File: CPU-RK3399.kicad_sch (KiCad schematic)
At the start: 0 parts

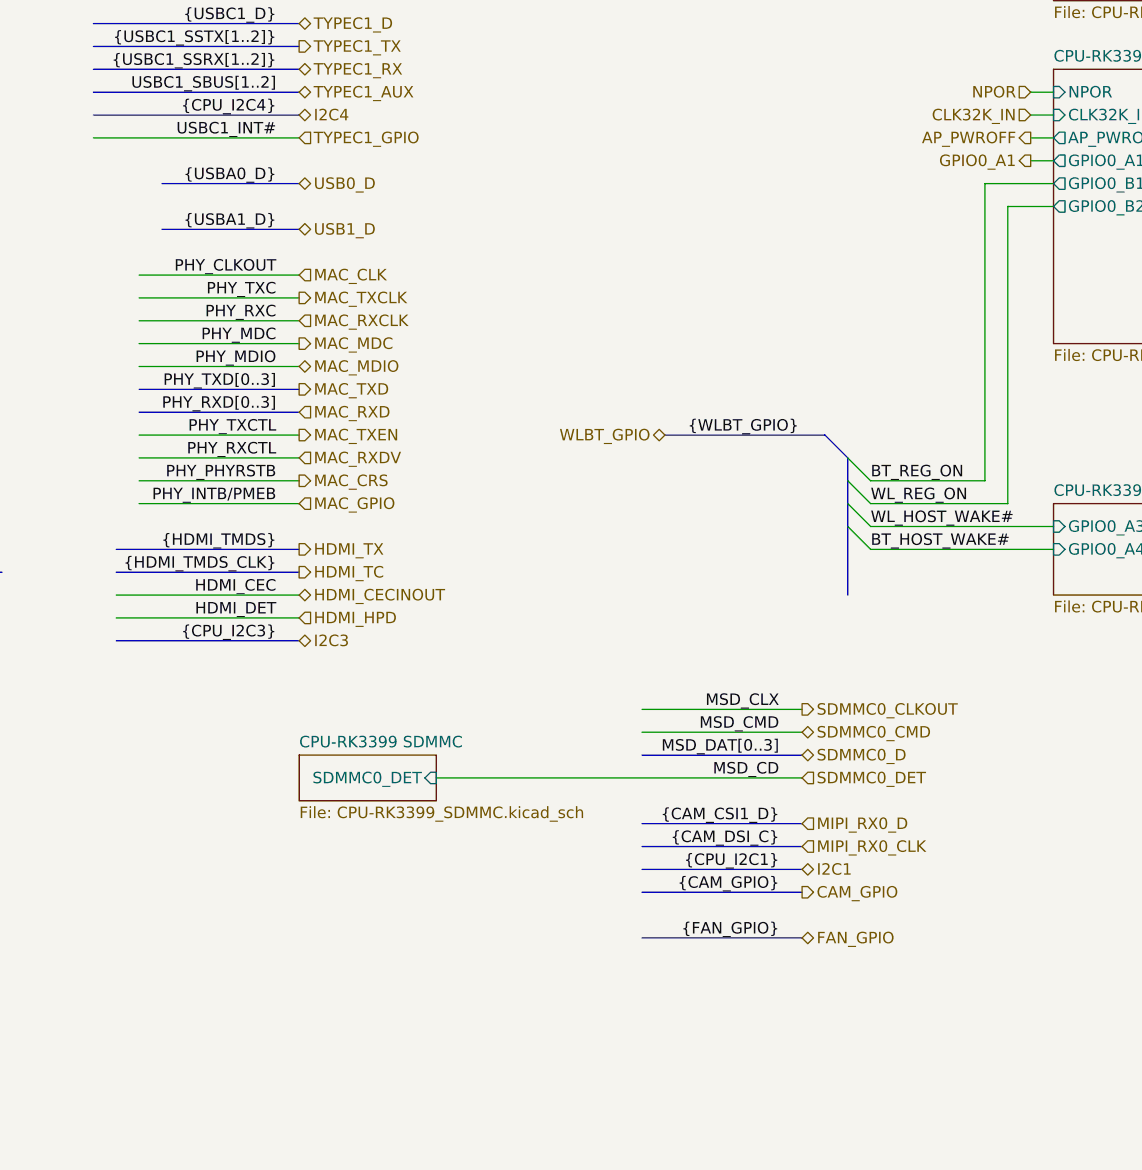
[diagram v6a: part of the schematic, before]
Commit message: design USB
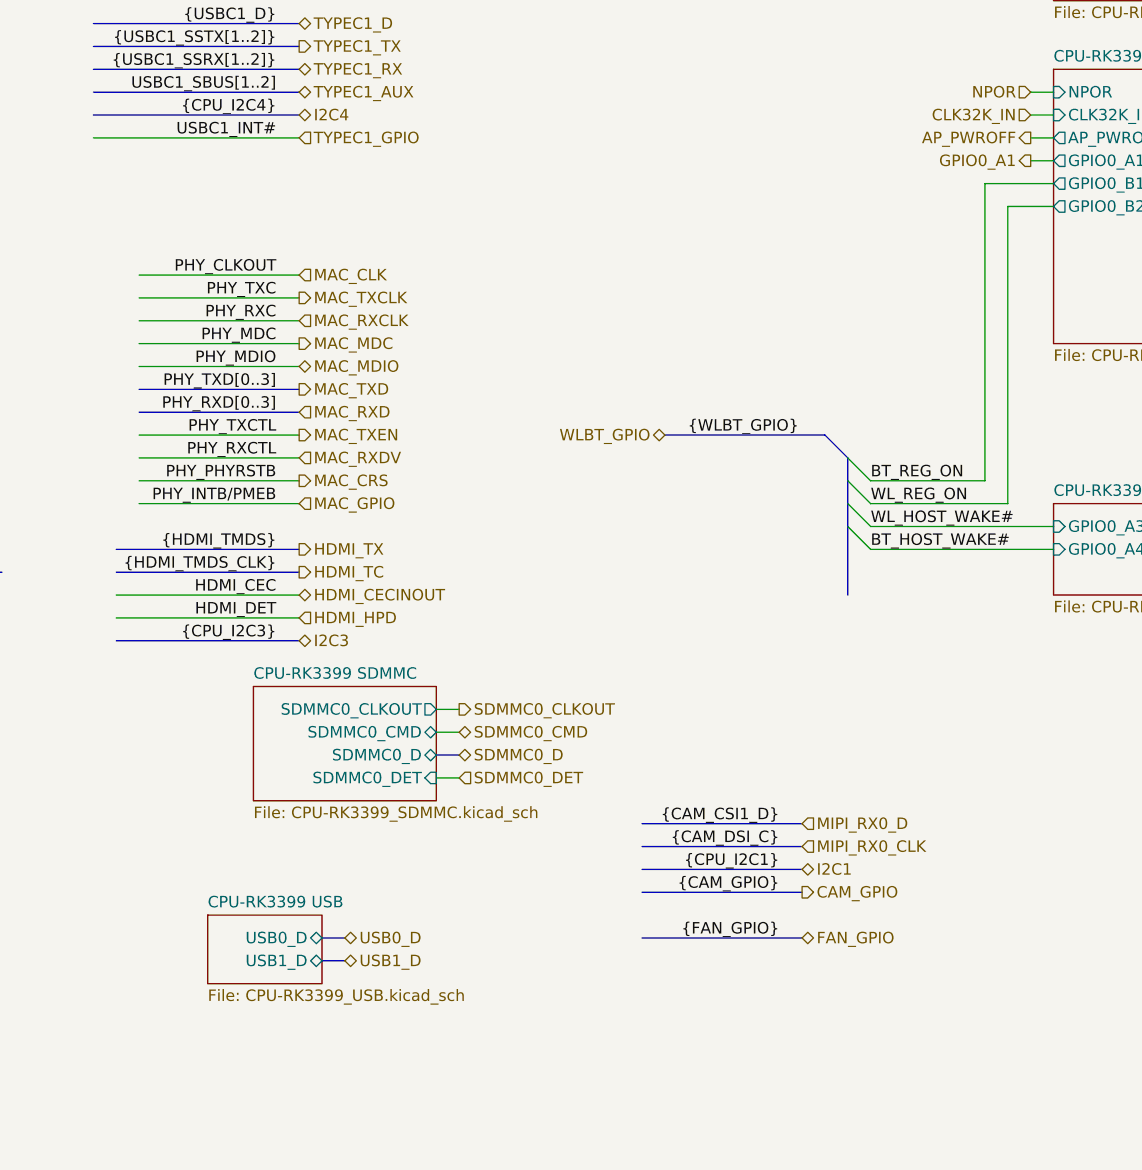
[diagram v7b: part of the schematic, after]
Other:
- added sheet CPU-RK3399 USB (CPU-RK3399_USB.kicad_sch)
- sheet CPU-RK3399 SDMMC ports: added SDMMC0_CLKOUT, SDMMC0_CMD, SDMMC0_D; removed none
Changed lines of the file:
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@@
 		)
 	)
-	(wire
-		(pts
-			(xy 208.28 134.62) (xy 190.5 134.62)
-		)
-		(stroke
-			(width 0)
-			(type default)
-		)
-	)
 	(bus
 		(pts
@@
 		)
 	)
-	(bus
-		(pts
-			(xy 137.16 73.66) (xy 152.4 73.66)
-		)
-		(stroke
-			(width 0)
-			(type default)
-		)
-	)
 	(wire
 		(pts
@@
 	(bus
 		(pts
+			(xy 154.94 160.02) (xy 157.48 160.02)
+		)
+		(stroke
+			(width 0)
+			(type default)
+		)
+	)
+	(bus
+		(pts
 			(xy 129.54 45.72) (xy 152.4 45.72)
 		)
@@
 		)
 	)
+	(bus
+		(pts
+			(xy 154.94 157.48) (xy 157.48 157.48)
+		)
+		(stroke
+			(width 0)
+			(type default)
+		)
+	)
 	(wire
 		(pts
@@
 	(bus
 		(pts
-			(xy 137.16 78.74) (xy 152.4 78.74)
+			(xy 71.12 147.32) (xy 73.66 147.32)
 		)
 		(stroke
@@
 		)
 	)
-	(bus
+	(wire
 		(pts
-			(xy 71.12 147.32) (xy 73.66 147.32)
+			(xy 167.64 139.7) (xy 170.18 139.7)
 		)
 		(stroke
@@
 	(bus
 		(pts
+			(xy 167.64 137.16) (xy 170.18 137.16)
+		)
+		(stroke
+			(width 0)
+			(type default)
+		)
+	)
+	(bus
+		(pts
 			(xy 129.54 55.88) (xy 152.4 55.88)
 		)
@@
 	(wire
 		(pts
-			(xy 81.28 50.8) (xy 83.82 50.8)
+			(xy 167.64 134.62) (xy 170.18 134.62)
 		)
 		(stroke
@@
 	(wire
 		(pts
-			(xy 152.4 91.44) (xy 134.62 91.44)
+			(xy 81.28 50.8) (xy 83.82 50.8)
 		)
 		(stroke
@@
 	(wire
 		(pts
-			(xy 208.28 132.08) (xy 190.5 132.08)
+			(xy 152.4 91.44) (xy 134.62 91.44)
 		)
 		(stroke
@@
 	(wire
 		(pts
-			(xy 167.64 139.7) (xy 208.28 139.7)
-		)
-		(stroke
-			(width 0)
-			(type default)
-		)
-	)
-	(bus
-		(pts
-			(xy 208.28 137.16) (xy 190.5 137.16)
-		)
-		(stroke
-			(width 0)
-			(type default)
-		)
-	)
-	(wire
-		(pts
 			(xy 71.12 160.02) (xy 73.66 160.02)
 		)
@@
 		)
 	)
+	(wire
+		(pts
+			(xy 167.64 132.08) (xy 170.18 132.08)
+		)
+		(stroke
+			(width 0)
+			(type default)
+		)
+	)
 	(bus
 		(pts
@@
 		)
 	)
-	(label "MSD_DAT[0..3]"
-		(at 205.74 137.16 180)
-		(effects
-			(font
-				(size 1.27 1.27)
-			)
-			(justify right bottom)
-		)
-	)
 	(label "{CPU_I2C4}"
 		(at 149.86 66.04 180)
@@
 		)
 	)
-	(label "MSD_CMD"
-		(at 205.74 134.62 180)
-		(effects
-			(font
-				(size 1.27 1.27)
-			)
-			(justify right bottom)
-		)
-	)
 	(label "{USBC0_SSRX[1..2]}"
 		(at 149.86 43.18 180)
@@
 		)
 	)
-	(label "MSD_CLX"
-		(at 205.74 132.08 180)
-		(effects
-			(font
-				(size 1.27 1.27)
-			)
-			(justify right bottom)
-		)
-	)
 	(label "CPU_SDIO0_INTN"
 		(at 99.06 129.54 180)
@@
 		)
 	)
-	(label "{USBA1_D}"
-		(at 149.86 78.74 180)
-		(effects
-			(font
-				(size 1.27 1.27)
-			)
-			(justify right bottom)
-		)
-	)
 	(label "{PCIe_PET[0..3]}"
 		(at 149.86 25.4 180)
@@
 		)
 	)
-	(label "MSD_CD"
-		(at 205.74 139.7 180)
-		(effects
-			(font
-				(size 1.27 1.27)
-			)
-			(justify right bottom)
-		)
-	)
 	(label "PHY_MDIO"
 		(at 149.86 93.98 180)
@@
 		)
 	)
-	(label "{USBA0_D}"
-		(at 149.86 73.66 180)
-		(effects
-			(font
-				(size 1.27 1.27)
-			)
-			(justify right bottom)
-		)
-	)
 	(hierarchical_label "EMMC"
 		(shape bidirectional)
@@
 	(hierarchical_label "USB1_D"
 		(shape bidirectional)
-		(at 152.4 78.74 0)
+		(at 157.48 160.02 0)
 		(effects
 			(font
@@
 	(hierarchical_label "USB0_D"
 		(shape bidirectional)
-		(at 152.4 73.66 0)
+		(at 157.48 157.48 0)
 		(effects
 			(font
@@
 	(hierarchical_label "SDMMC0_CLKOUT"
 		(shape output)
-		(at 208.28 132.08 0)
+		(at 170.18 132.08 0)
 		(effects
 			(font
@@
 	(hierarchical_label "SDMMC0_DET"
 		(shape input)
-		(at 208.28 139.7 0)
+		(at 170.18 139.7 0)
 		(effects
 			(font
@@
 	(hierarchical_label "SDMMC0_CMD"
 		(shape bidirectional)
-		(at 208.28 134.62 0)
+		(at 170.18 134.62 0)
 		(effects
 			(font
@@
 	(hierarchical_label "SDMMC0_D"
 		(shape bidirectional)
-		(at 208.28 137.16 0)
+		(at 170.18 137.16 0)
 		(effects
 			(font
@@
 	)
 	(sheet
+		(at 142.24 154.94)
+		(size 12.7 7.62)
+		(exclude_from_sim no)
+		(in_bom yes)
+		(on_board yes)
+		(dnp no)
+		(fields_autoplaced yes)
+		(stroke
+			(width 0.1524)
+			(type solid)
+		)
+		(fill
+			(color 0 0 0 0.0000)
+		)
+		(property "Sheetname" "CPU-RK3399 USB"
+			(at 142.24 154.2284 0)
+			(effects
+				(font
+					(size 1.27 1.27)
+				)
+				(justify left bottom)
+			)
+		)
+		(property "Sheetfile" "CPU-RK3399_USB.kicad_sch"
+			(at 142.24 163.1446 0)
+			(effects
+				(font
+					(size 1.27 1.27)
+				)
+				(justify left top)
+			)
+		)
+		(pin "USB1_D" bidirectional
+			(at 154.94 160.02 0)
+			(effects
+				(font
+					(size 1.27 1.27)
+				)
+				(justify right)
+			)
+		)
+		(pin "USB0_D" bidirectional
+			(at 154.94 157.48 0)
+			(effects
+				(font
+					(size 1.27 1.27)
+				)
+				(justify right)
+			)
+		)
+		(instances
+			(project "VESA-SBC3399"
+				(path "/ebc9dc57-8b05-484a-a5cd-c53b1efc71d3/a7299b18-4123-434b-8c69-0b9524fffa12"
+					(page "26")
+				)
+			)
+		)
+	)
+	(sheet
 		(at 236.22 109.22)
 		(size 17.78 10.16)
@@
 	)
 	(sheet
-		(at 152.4 137.16)
-		(size 15.24 5.08)
+		(at 147.32 129.54)
+		(size 20.32 12.7)
 		(exclude_from_sim no)
 		(in_bom yes)
@@
 		)
 		(property "Sheetname" "CPU-RK3399 SDMMC"
-			(at 152.4 136.4484 0)
+			(at 147.32 128.8284 0)
 			(effects
 				(font
@@
 		)
 		(property "Sheetfile" "CPU-RK3399_SDMMC.kicad_sch"
-			(at 152.4 142.8246 0)
+			(at 147.32 142.8246 0)
 			(effects
 				(font
@@
 			(effects
 				(font
+					(size 1.27 1.27)
+				)
+				(justify right)
+			)
+		)
+		(pin "SDMMC0_CMD" bidirectional
+			(at 167.64 134.62 0)
+			(effects
+				(font
+					(size 1.27 1.27)
+				)
+				(justify right)
+			)
+		)
+		(pin "SDMMC0_D" bidirectional
+			(at 167.64 137.16 0)
+			(effects
+				(font
+					(size 1.27 1.27)
+				)
+				(justify right)
+			)
+		)
+		(pin "SDMMC0_CLKOUT" output
+			(at 167.64 132.08 0)
+			(effects
+				(font

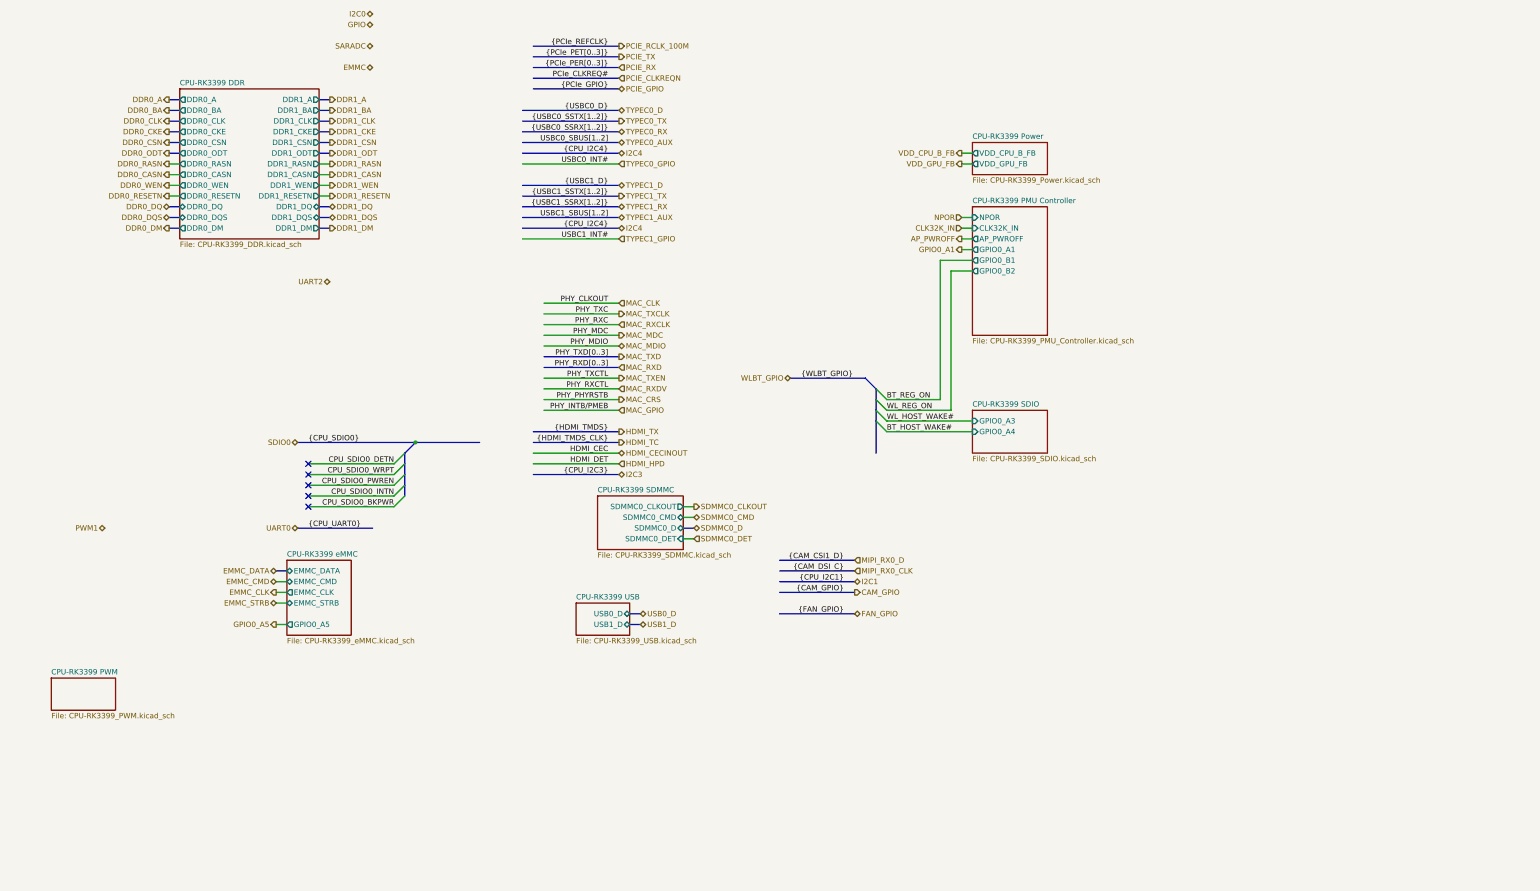
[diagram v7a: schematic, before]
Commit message: update schematic
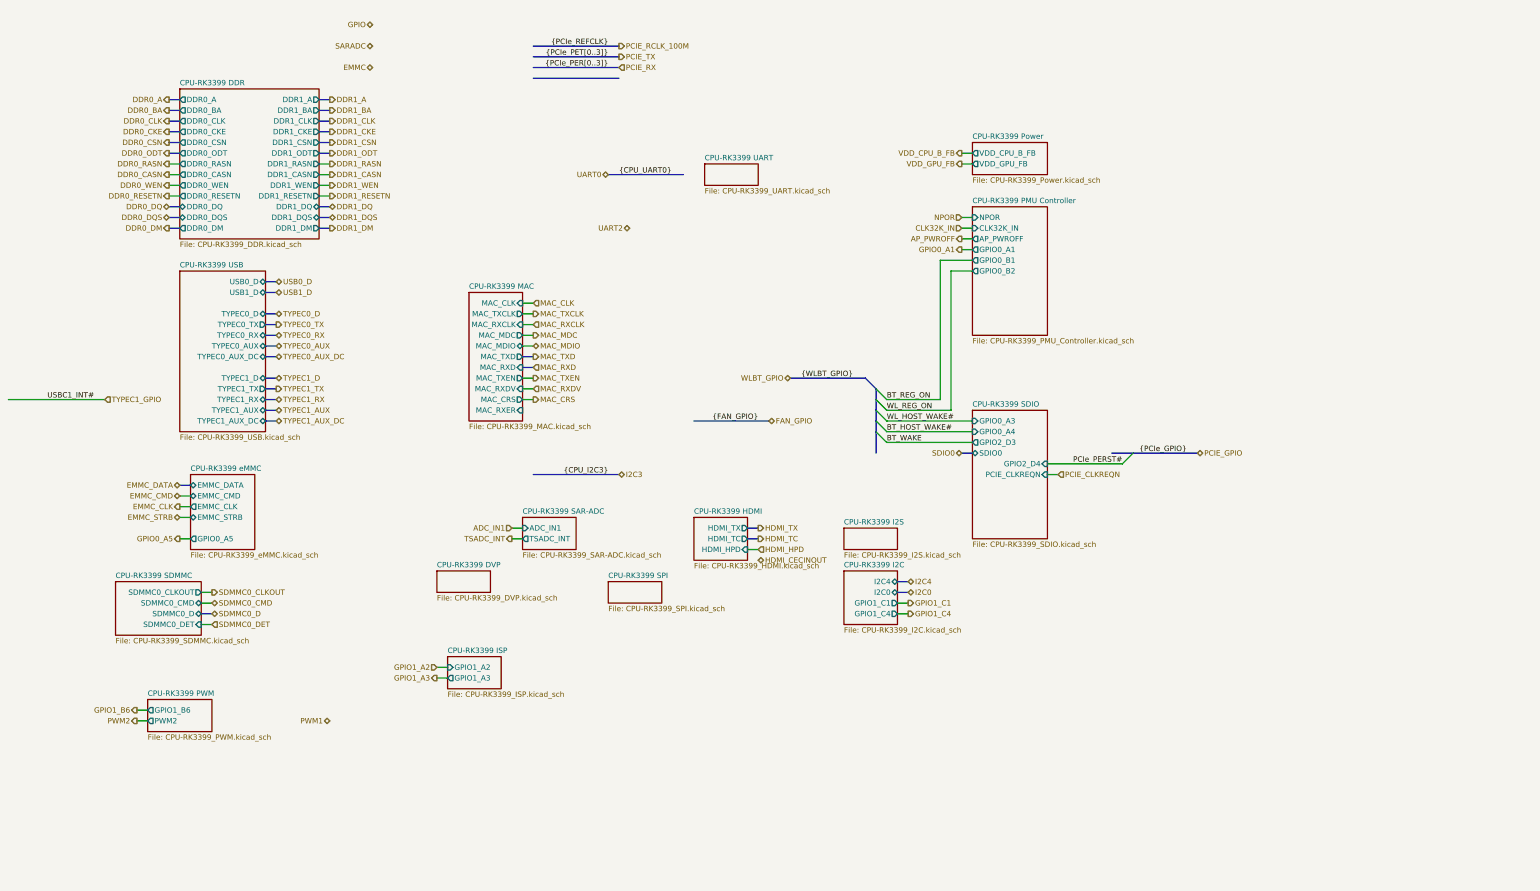
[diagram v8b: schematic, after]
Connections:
- no-connect marks 5 -> 0
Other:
- added sheet CPU-RK3399 DVP (CPU-RK3399_DVP.kicad_sch)
- added sheet CPU-RK3399 HDMI (CPU-RK3399_HDMI.kicad_sch)
- added sheet CPU-RK3399 I2C (CPU-RK3399_I2C.kicad_sch)
- added sheet CPU-RK3399 I2S (CPU-RK3399_I2S.kicad_sch)
- added sheet CPU-RK3399 ISP (CPU-RK3399_ISP.kicad_sch)
- added sheet CPU-RK3399 MAC (CPU-RK3399_MAC.kicad_sch)
- added sheet CPU-RK3399 SAR-ADC (CPU-RK3399_SAR-ADC.kicad_sch)
- added sheet CPU-RK3399 SPI (CPU-RK3399_SPI.kicad_sch)
- added sheet CPU-RK3399 UART (CPU-RK3399_UART.kicad_sch)
- sheet CPU-RK3399 PWM ports: added GPIO1_B6, PWM2; removed none
- sheet CPU-RK3399 SDIO ports: added GPIO2_D3, GPIO2_D4, PCIE_CLKREQN, SDIO0; removed none
- sheet CPU-RK3399 USB ports: added TYPEC0_AUX, TYPEC0_AUX_DC, TYPEC0_D, TYPEC0_RX, TYPEC0_TX, TYPEC1_AUX, TYPEC1_AUX_DC, TYPEC1_D, TYPEC1_RX, TYPEC1_TX; removed none
